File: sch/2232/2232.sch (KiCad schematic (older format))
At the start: 58 parts, among them J1 47346-0001, J2 IDC-06, J3 IDC-06, J4 IDC-10, J5 IDC-10, J6 6P6C, J7 Screw_Terminal_01x06, J8 Screw_Terminal_01x06, U1 FT2232D, U2 AMS1117-3.3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

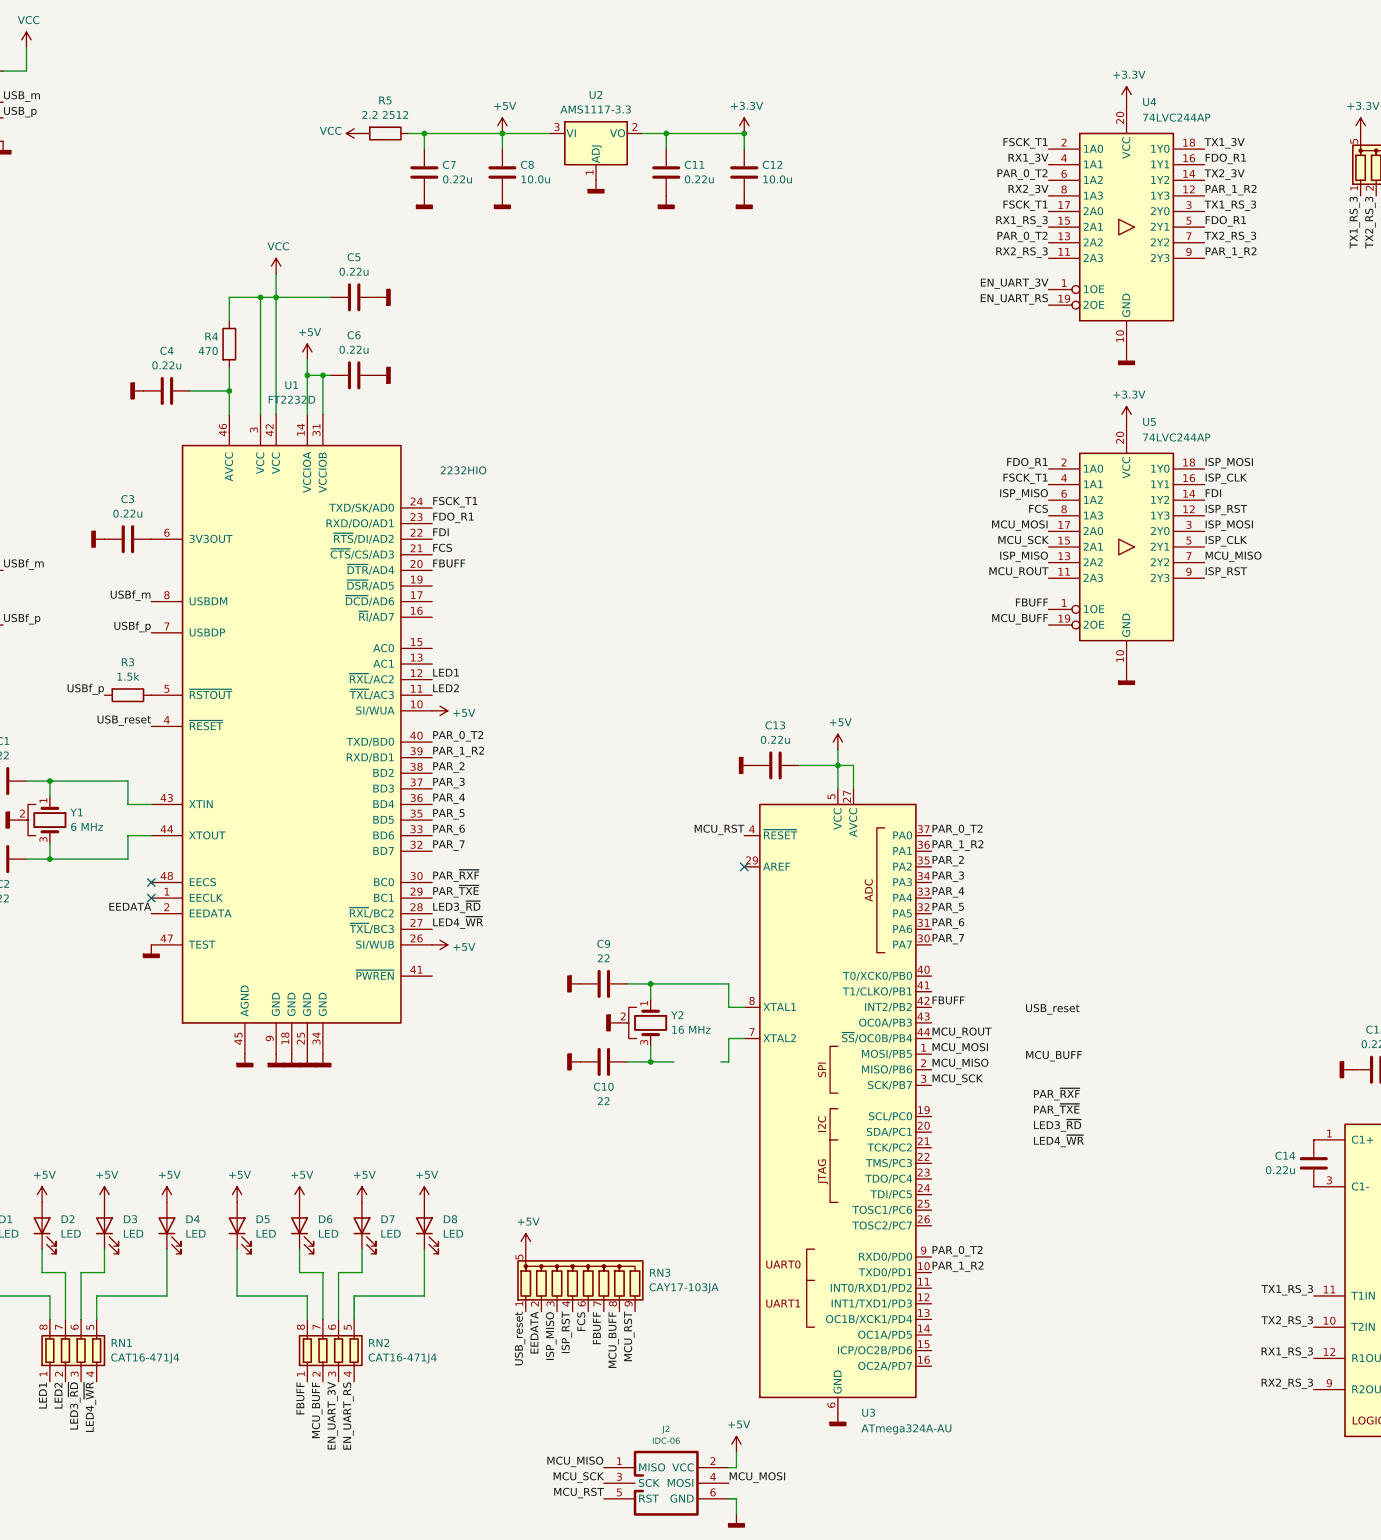
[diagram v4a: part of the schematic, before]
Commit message: UART multiplexing
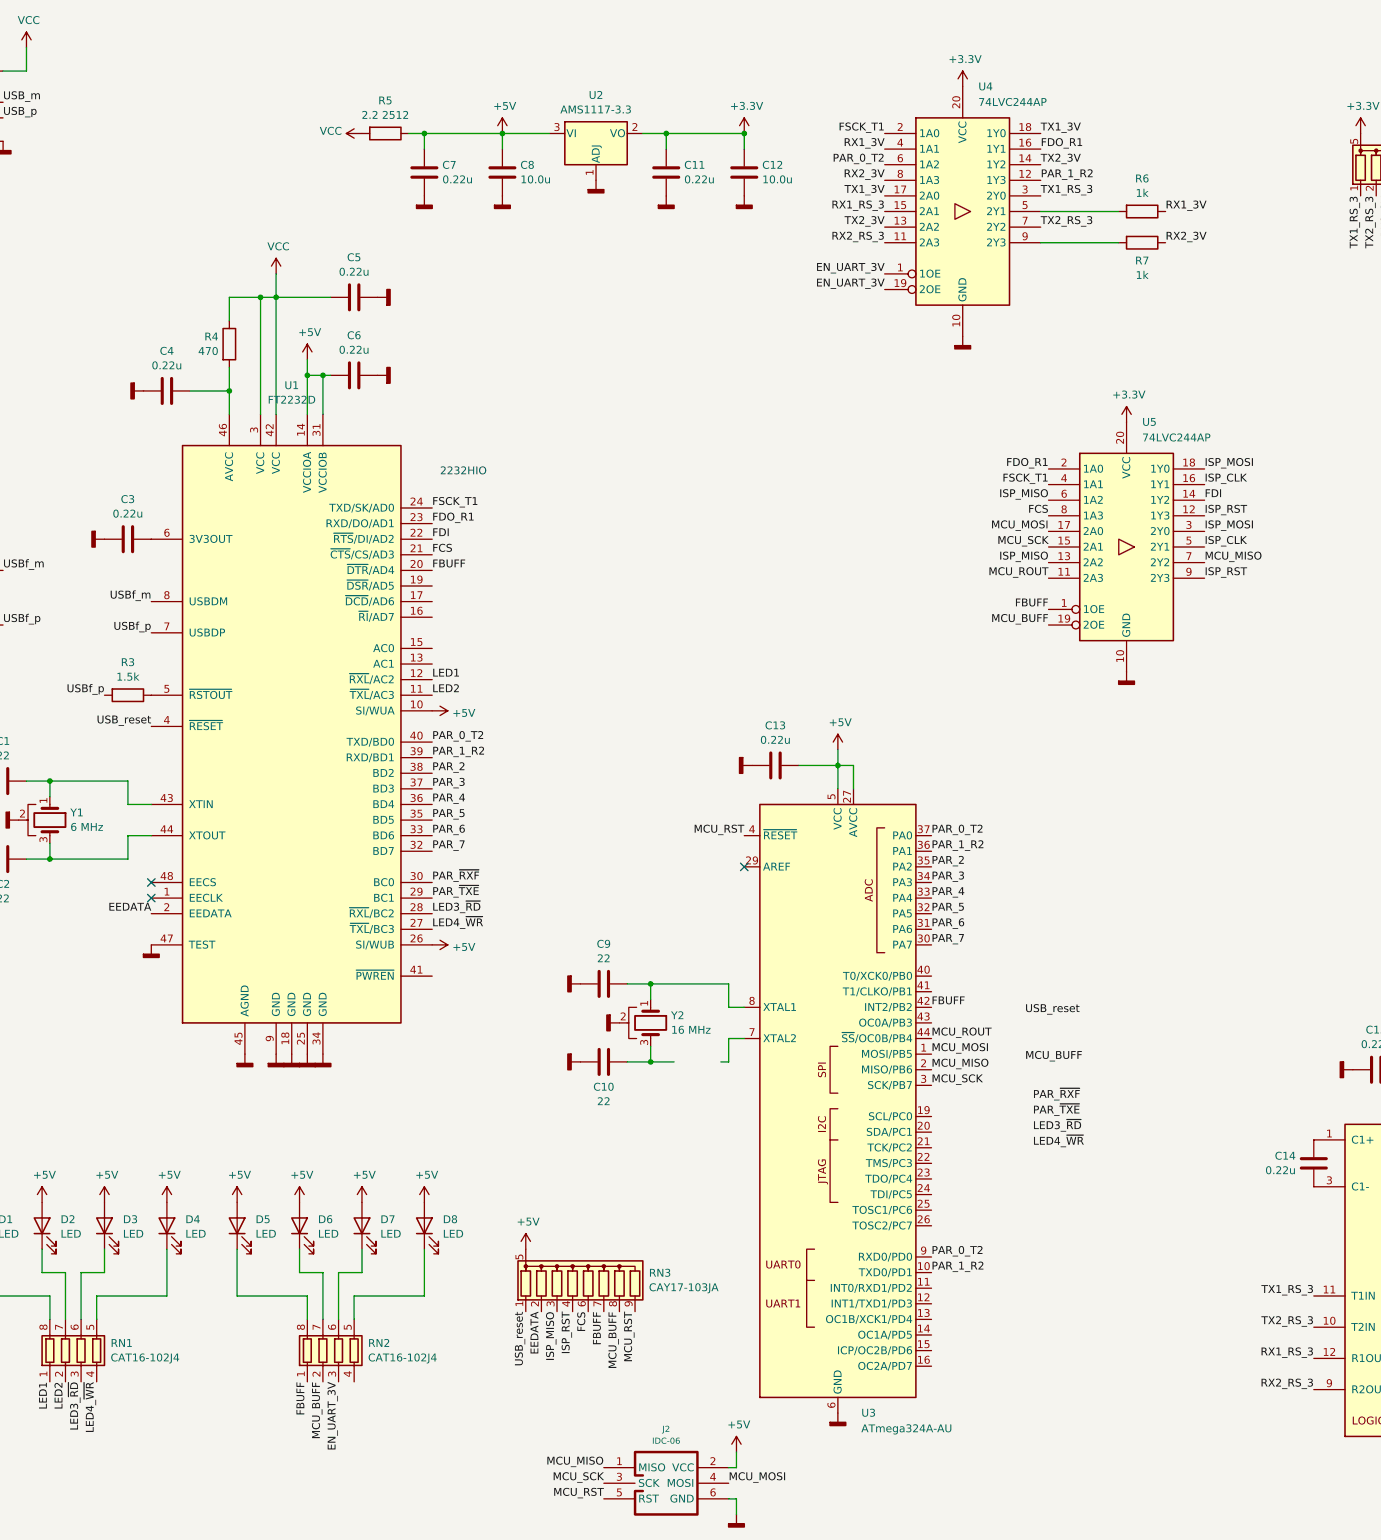
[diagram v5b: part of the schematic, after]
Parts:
- added R6, R7: 1k, NevaDA:R_0603, symbol Device:R
- RN1, RN2: value CAT16-471J4 -> CAT16-102J4
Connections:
- net EN_UART_3V: now also U4.19 (2OE)
- net EN_UART_RS: no longer RN2.4 (R4.1), U4.19 (2OE)
- net FDO_R1: no longer U4.5 (2Y1)
- net FSCK_T1: no longer U4.17 (2A0)
- net PAR_0_T2: no longer U4.13 (2A2)
- net PAR_1_R2: no longer U4.9 (2Y3)
- net RX1_3V: now also R6.1
- net RX2_3V: now also R7.1
- net TX1_3V: now also U4.17 (2A0)
- net TX2_3V: now also U4.13 (2A2)
- new net: R6.2, U4.5 (2Y1)
- new net: R7.2, U4.9 (2Y3)
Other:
- moved on the sheet: U4
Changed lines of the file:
@@
 L symbol:74LVC244D U4
 U 1 1 5FD54B9A
-P 8750 2250
-F 0 "U4" H 8850 3050 50  0000 L CNN
-F 1 "74LVC244AP" H 8850 2950 50  0000 L CNN
-F 2 "NevaDA:TSSOP-20" H 8750 2250 50  0001 C CNN
-F 3 "http://www.ti.com/lit/gpn/sn74LVC125" H 8750 2250 50  0001 C CNN
-	1    8750 2250
+P 7700 2150
+F 0 "U4" H 7800 2950 50  0000 L CNN
+F 1 "74LVC244AP" H 7800 2850 50  0000 L CNN
+F 2 "NevaDA:TSSOP-20" H 7700 2150 50  0001 C CNN
+F 3 "http://www.ti.com/lit/gpn/sn74LVC125" H 7700 2150 50  0001 C CNN
+	1    7700 2150
 	1    0    0    -1
 $EndComp
@@
 L power:+3.3V #PWR0127
 U 1 1 5FDC40BD
-P 8750 1450
-F 0 "#PWR0127" H 8750 1300 50  0001 C CNN
-F 1 "+3.3V" H 8765 1625 50  0000 C CNN
-F 2 "" H 8750 1450 50  0001 C CNN
-F 3 "" H 8750 1450 50  0001 C CNN
-	1    8750 1450
+P 7700 1350
+F 0 "#PWR0127" H 7700 1200 50  0001 C CNN
+F 1 "+3.3V" H 7715 1525 50  0000 C CNN
+F 2 "" H 7700 1350 50  0001 C CNN
+F 3 "" H 7700 1350 50  0001 C CNN
+	1    7700 1350
 	1    0    0    -1
 $EndComp
@@
 L power:GNDD #PWR0128
 U 1 1 5FDC4ABB
-P 8750 3050
-F 0 "#PWR0128" H 8750 2800 50  0001 C CNN
-F 1 "GNDD" V 8754 2940 50  0001 R CNN
-F 2 "" H 8750 3050 50  0001 C CNN
-F 3 "" H 8750 3050 50  0001 C CNN
-	1    8750 3050
-	1    0    0    -1
-$EndComp
-Text Label 8250 1950 2    50   ~ 0
+P 7700 2950
+F 0 "#PWR0128" H 7700 2700 50  0001 C CNN
+F 1 "GNDD" V 7704 2840 50  0001 R CNN
+F 2 "" H 7700 2950 50  0001 C CNN
+F 3 "" H 7700 2950 50  0001 C CNN
+	1    7700 2950
+	1    0    0    -1
+$EndComp
+Text Label 7200 1850 2    50   ~ 0
 PAR_0_T2
-Text Label 9250 2050 0    50   ~ 0
+Text Label 8200 1950 0    50   ~ 0
 PAR_1_R2
-Text Label 8250 2350 2    50   ~ 0
-PAR_0_T2
-Text Label 9250 2450 0    50   ~ 0
-PAR_1_R2
-Text Label 8250 2650 2    50   ~ 0
+Text Label 7200 2550 2    50   ~ 0
 EN_UART_3V
-Text Label 8250 2750 2    50   ~ 0
-EN_UART_RS
 Text Label 13700 5050 2    50   ~ 0
 TX1_3V
-Text Label 9250 1950 0    50   ~ 0
+Text Label 8200 1850 0    50   ~ 0
 TX2_3V
 Text Label 13700 5250 2    50   ~ 0
@@
 Text Label 13700 5350 2    50   ~ 0
 RX2_3V
-Text Label 8250 1850 2    50   ~ 0
+Text Label 7200 1750 2    50   ~ 0
 RX1_3V
-Text Label 8250 2050 2    50   ~ 0
+Text Label 7200 1950 2    50   ~ 0
 RX2_3V
-Text Label 9250 1750 0    50   ~ 0
+Text Label 8200 1650 0    50   ~ 0
 TX1_3V
-Text Label 9250 2150 0    50   ~ 0
+Text Label 8200 2050 0    50   ~ 0
 TX1_RS_3
-Text Label 9250 2350 0    50   ~ 0
+Text Label 8200 2250 0    50   ~ 0
 TX2_RS_3
-Text Label 8250 2450 2    50   ~ 0
-RX2_RS_3
-Text Label 8250 2250 2    50   ~ 0
-RX1_RS_3
 Text Label 9950 9500 2    50   ~ 0
 RX1_RS_3
@@
 Text Label 4300 4250 0    50   ~ 0
 FDI
-Text Label 8250 1750 2    50   ~ 0
+Text Label 7200 1650 2    50   ~ 0
 FSCK_T1
-Text Label 9250 1850 0    50   ~ 0
-FDO_R1
-Text Label 8250 2150 2    50   ~ 0
-FSCK_T1
-Text Label 9250 2250 0    50   ~ 0
+Text Label 8200 1750 0    50   ~ 0
 FDO_R1
 Text Label 4300 4350 0    50   ~ 0
@@
 P 2050 9450
 F 0 "RN1" H 2239 9497 50  0000 L CNN
-F 1 "CAT16-471J4" H 2239 9404 50  0000 L CNN
+F 1 "CAT16-102J4" H 2239 9404 50  0000 L CNN
 F 2 "NevaDA:R_CAT-16-4" V 2325 9450 50  0001 C CNN
 F 3 "~" H 2050 9450 50  0001 C CNN
@@
 P 3700 9450
 F 0 "RN2" H 3889 9497 50  0000 L CNN
-F 1 "CAT16-471J4" H 3889 9404 50  0000 L CNN
+F 1 "CAT16-102J4" H 3889 9404 50  0000 L CNN
 F 2 "NevaDA:R_CAT-16-4" V 3975 9450 50  0001 C CNN
 F 3 "~" H 3700 9450 50  0001 C CNN
@@
 Text Label 3700 9650 3    50   ~ 0
 EN_UART_3V
-Text Label 3800 9650 3    50   ~ 0
-EN_UART_RS
 Text Label 3600 9650 3    50   ~ 0
 MCU_BUFF
@@
 Wire Wire Line
 	6650 5700 6900 5700
+Text Label 7200 2250 2    50   ~ 0
+TX2_3V
+Text Label 7200 2050 2    50   ~ 0
+TX1_3V
+$Comp
+L Device:R R6
+U 1 1 5FDBB780
+P 8850 2150
+F 0 "R6" V 8640 2150 50  0000 C CNN
+F 1 "1k" V 8733 2150 50  0000 C CNN
+F 2 "NevaDA:R_0603" V 8780 2150 50  0001 C CNN
+F 3 "~" H 8850 2150 50  0001 C CNN
+	1    8850 2150
+	0    1    1    0
+$EndComp
+Text Label 9000 2150 0    50   ~ 0
+RX1_3V
+Text Label 9000 2350 0    50   ~ 0
+RX2_3V
+$Comp
+L Device:R R7
+U 1 1 5FDC231A
+P 8850 2350
+F 0 "R7" V 8966 2350 50  0000 C CNN
+F 1 "1k" V 9059 2350 50  0000 C CNN
+F 2 "NevaDA:R_0603" V 8780 2350 50  0001 C CNN
+F 3 "~" H 8850 2350 50  0001 C CNN
+	1    8850 2350
+	0    1    1    0
+$EndComp
+Wire Wire Line
+	8700 2350 8200 2350
+Wire Wire Line
+	8200 2150 8700 2150
+Text Label 7200 2150 2    50   ~ 0
+RX1_RS_3
+Text Label 7200 2350 2    50   ~ 0
+RX2_RS_3
+Text Label 7200 2650 2    50   ~ 0
+EN_UART_3V
 $EndSCHEMATC

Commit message: Routing started
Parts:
- removed U7: 74HC138, NevaDA:SOIC-16, symbol 2232-rescue:74HC138-symbol
- added D10: S3M, symbol Device:D
- added Q1, Q2: Q_NPN_BEC, symbol Device:Q_NPN_BEC
- added R10: 1M, NevaDA:R_0603, symbol Device:R
- added R8: 100, symbol Device:R
- added R9: 2.2 2512, symbol Device:R
- added V1, V2, V3, V4: Virtual, NevaDA:StickyPad_13mm, symbol symbol:Virtual
- D1: Role (none) -> Rx1
- D2: Role (none) -> Tx1
- D3: Role (none) -> Rx2
- D4: Role (none) -> Tx2
- D5: Role (none) -> UART
- D6: Role (none) -> FPROG
- D7: Role (none) -> MPROG
- D8: Role (none) -> BUSY
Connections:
- net +3V3: now also R8.2
- net +5V: now also RN1.1 (R1.1), RN1.2 (R2.1), RN1.3 (R3.1), RN1.4 (R4.1), RN2.1 (R1.1), RN2.2 (R2.1), RN2.3 (R3.1), RN2.4 (R4.1), D10.2 (A); no longer D1.2 (A), D2.2 (A), D3.2 (A), D4.2 (A), D5.2 (A), D6.2 (A), D7.2 (A), D8.2 (A)
- net FBUFF: now also D6.1 (K); no longer RN2.1 (R1.1)
- net GNDD: now also R10.2
- net IDC_VCC: now also Q1.2 (E), R9.2
- net LED1: now also D1.1 (K); no longer RN1.1 (R1.1)
- net LED2: now also D2.1 (K); no longer RN1.2 (R2.1)
- net LED3_~RD: now also D3.1 (K), U1.17 (~DCD~/AD6), U3.13 (OC1B/XCK1/PD4); no longer RN1.3 (R3.1)
- net LED4_~WR: now also D4.1 (K), U1.16 (~RI~/AD7), U3.14 (OC1A/PD5); no longer RN1.4 (R4.1)
- net MCU_BUFF: now also D7.1 (K), U3.43 (OC0A/PB3); no longer RN2.2 (R2.1)
- net PAR_~RXF: now also U3.11 (INT0/RXD1/PD2)
- net PAR_~TXE: now also U3.12 (INT1/TXD1/PD3)
- net USB_reset: now also U3.15 (ICP/OC2B/PD6)
- net USBf_p: no longer R2.1, U1.7 (USBDP)
- net at J1.5 (Shield): now also R10.1
- net MCU_LED: now reaches U3.16 (OC2A/PD7)
- net MCU_LED: now also D8.1 (K)
- net at U3.7 (XTAL2): now also C10.1, Y2.3
- net at RN1.8 (R1.2): now also D4.2 (A); no longer D1.1 (K)
- net at RN1.7 (R2.2): now also D3.2 (A); no longer D2.1 (K)
- net at RN1.6 (R3.2): now also D2.2 (A); no longer D3.1 (K)
- net at RN1.5 (R4.2): now also D1.2 (A); no longer D4.1 (K)
- net at RN2.8 (R1.2): now also D8.2 (A); no longer D5.1 (K)
- net at RN2.7 (R2.2): now also D7.2 (A); no longer D6.1 (K)
- net at RN2.6 (R3.2): now also D6.2 (A); no longer D7.1 (K)
- net at RN2.5 (R4.2): now also D5.2 (A); no longer D8.1 (K)
- net EN_UART_3V renamed EN_UART
- net EN_UART: now also D5.1 (K); no longer RN2.3 (R3.1)
- net USB_m renamed USB_D-
- net USB_p renamed USB_D+
- net USBf_m renamed USBf_D-
- new net: Q1.3 (C), Q2.1 (B), R8.1
- new net: Q1.1 (B), Q2.2 (E), R9.1
- new net: D10.1 (K), Q2.3 (C)
- new net USBf_D+: R2.1, U1.7 (USBDP)
- no-connect marks 5 -> 8
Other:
- note added: "Modes of operation:\nUSB-2xUART - in idle (general purpose + ESP prog.)\n232HIO programmer (when FBUFF asserted)\nMCU-assisted programmer (when PC sends special instruction)\n"
- moved on the sheet: D1, D2, D3, D4, D5, D6, D7, D8, R6, R7, RN1, RN2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
